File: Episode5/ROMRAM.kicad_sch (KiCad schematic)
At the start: 23 parts, among them SW1 Bank, SW2 RST SW, U10 AS6C1008, U11 HD63C09P, U12 MIC1232, U9 SST39SF010, X1 12MHz

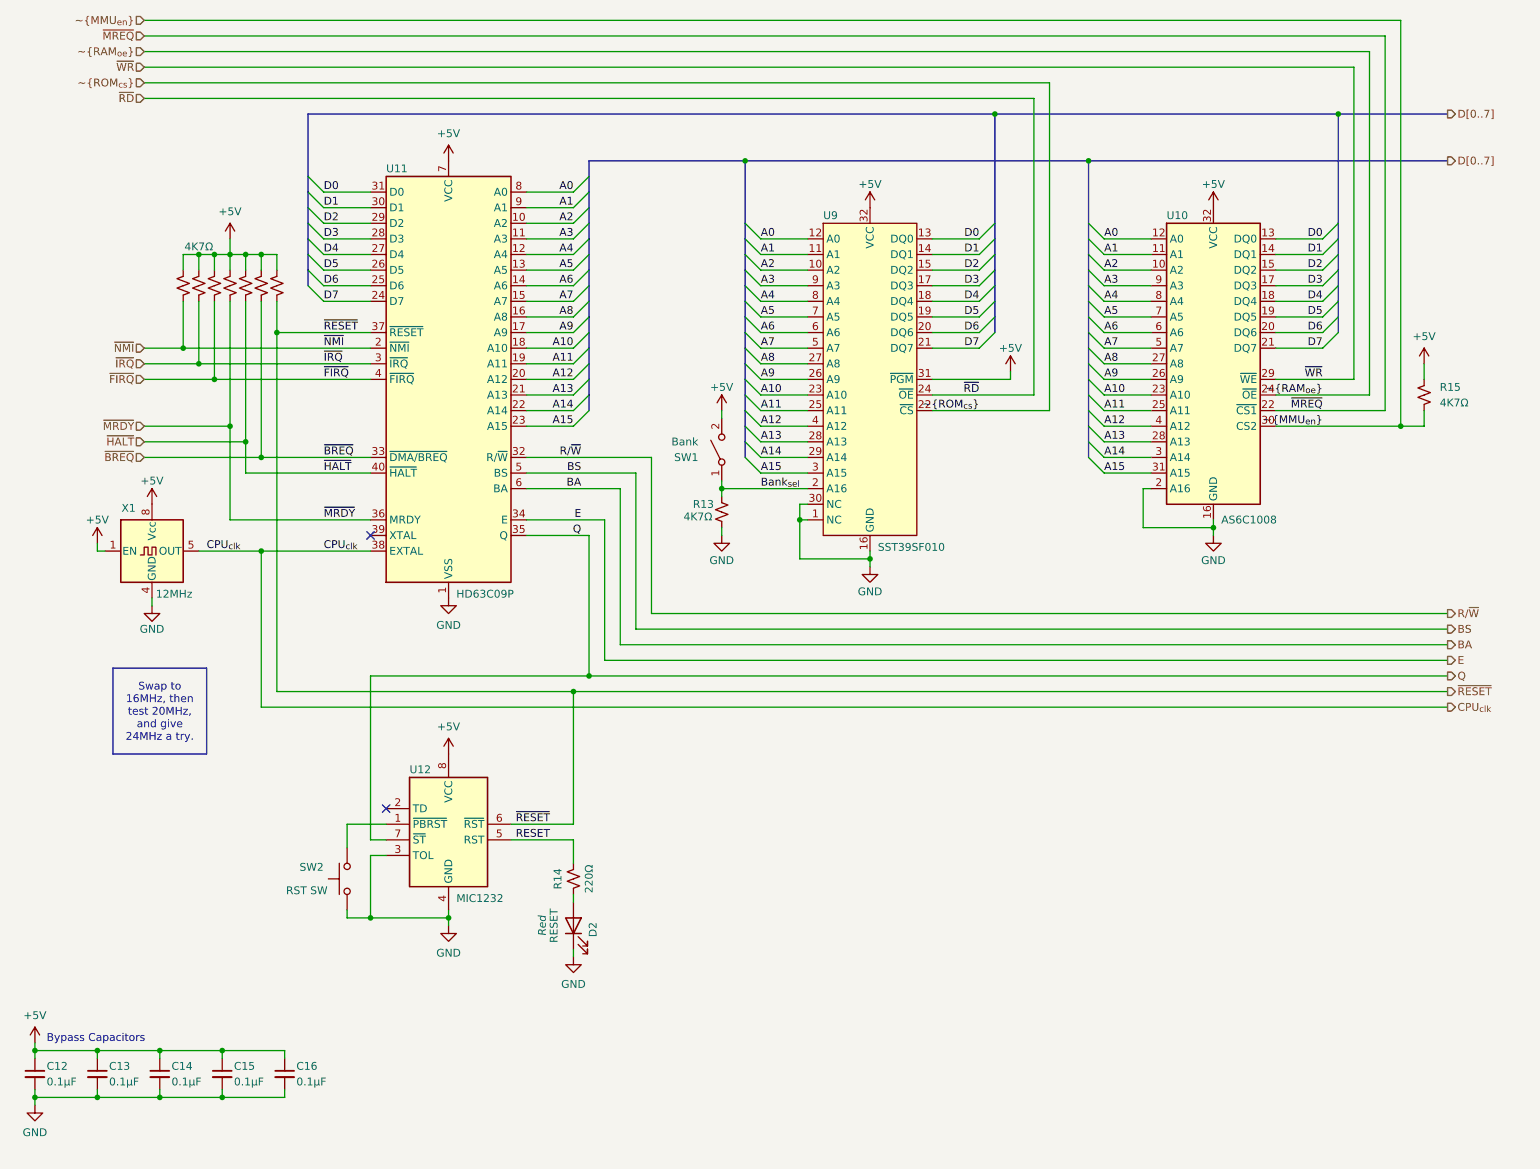
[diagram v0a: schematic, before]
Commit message: Placed Global labels instead. And toying with new PLDs
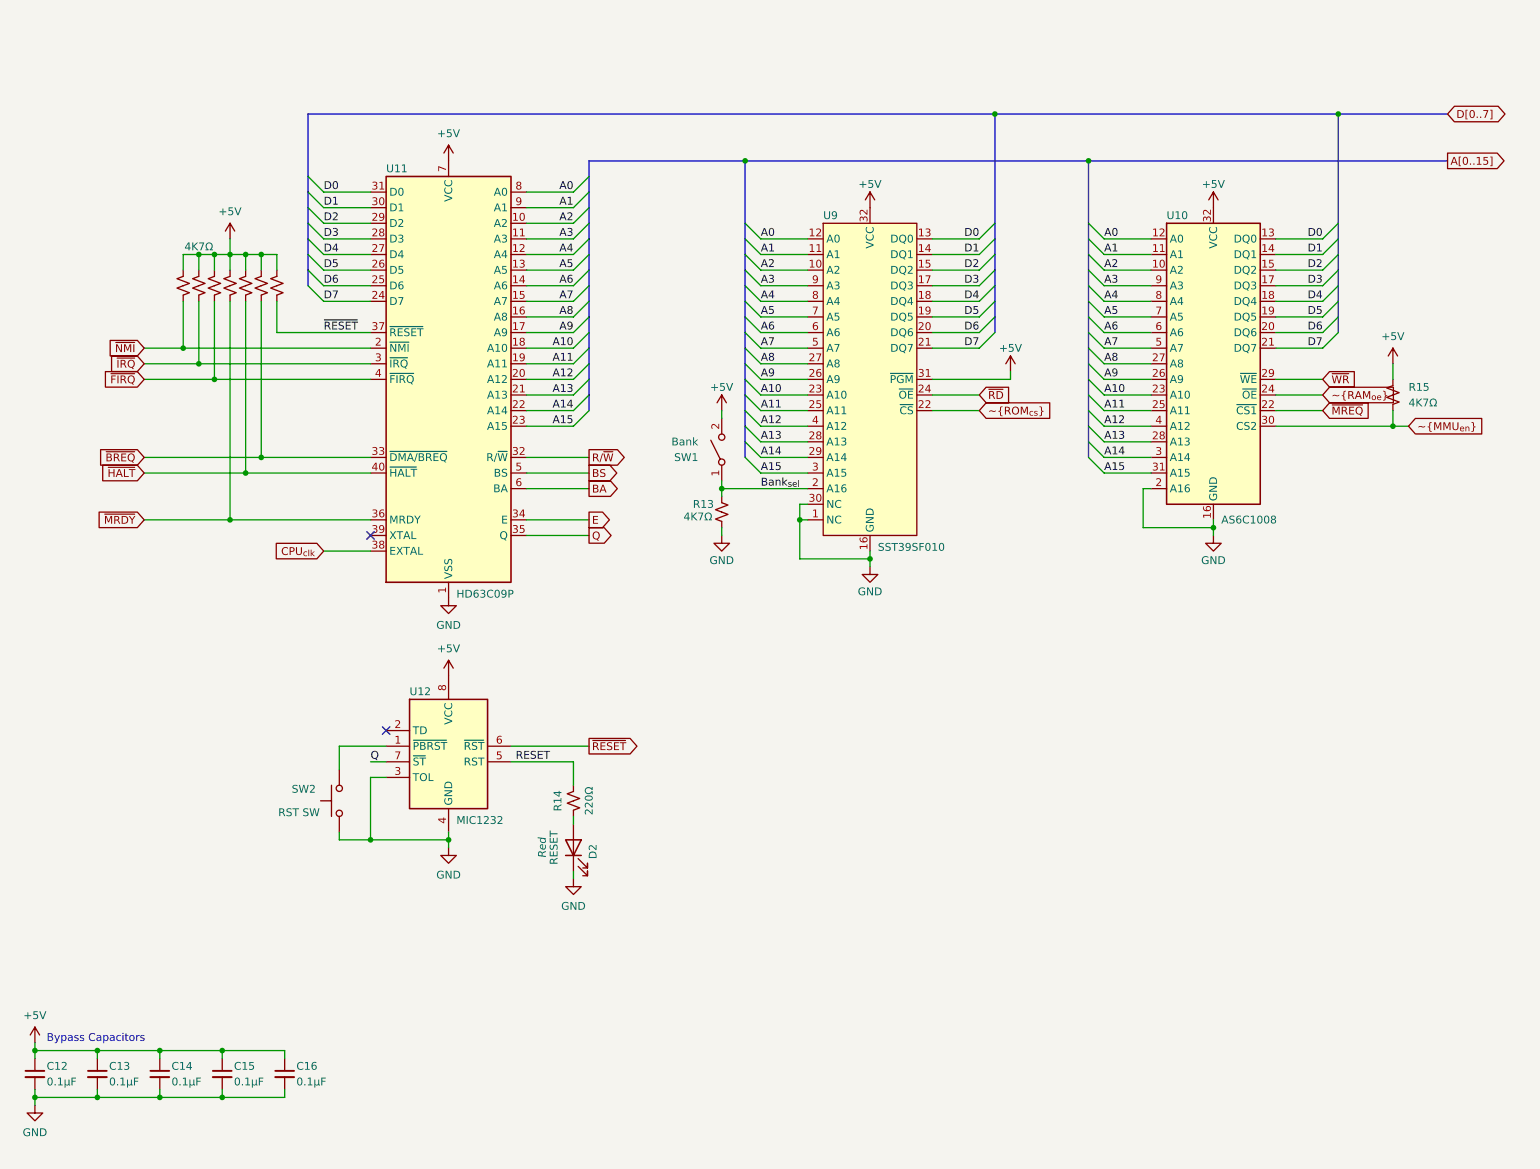
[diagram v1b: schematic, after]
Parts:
- removed X1: 12MHz, Oscillator:Oscillator_DIP-8, symbol Oscillator:CXO_DIP8
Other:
- moved on the sheet: D2, R14, R15, SW2, U12

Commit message: Toying with different alternatives for the CPU board
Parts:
- added X1: 16MHz, Oscillator:Oscillator_DIP-8, symbol Oscillator:CXO_DIP8
- renumbered C12 to C1, C13 to C2, C14 to C3, C15 to C4, C16 to C5, D2 to D1, R6 to R1, R14 to R10, R7 to R2, R8 to R3, R9 to R4, R10 to R5, R11 to R6, R12 to R7, R15 to R8, R13 to R9, U9 to U1, U10 to U2, U11 to U3, U12 to U4
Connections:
- net +5V: now also X1.1 (EN), X1.8 (Vcc)
- net CPU_{clk}: now also X1.5 (OUT)
- net GND: now also X1.4 (GND)
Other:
- moved on the sheet: D1, R10, SW2, U4

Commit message: Finished the preliminary design of the CPU card
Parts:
- removed C4, C5: 0.1µF, symbol Device:C_Small
- removed D1: RESET, symbol Device:LED
- removed R1, R2, R3, R4, R5, R6, R7: 4K7Ω, symbol Device:R_Small_US
- removed R10: 220Ω, symbol Device:R_Small_US
- removed SW2: RST SW, symbol Switch:SW_Push
- removed U3: HD63C09P, Package_DIP:DIP-40_W15.24mm_Socket, symbol CPU_NXP_6800:MC6809
- removed U4: MIC1232, Package_DIP:DIP-8_W7.62mm_Socket, symbol MicroHobbyist:MIC1232
- removed X1: 16MHz, Oscillator:Oscillator_DIP-8, symbol Oscillator:CXO_DIP8
- added JP1: CLR NVRAM, Connector_PinHeader_2.54mm:PinHeader_1x02_P2.54mm_Vertical, symbol Jumper:Jumper_2_Small_Open
- added U14: DS12C887A, Package_DIP:DIP-24_W15.24mm_Socket_LongPads, symbol 6309 Unleashed 2.0:DS12C887A
- SW3: renamed from SW1; value Bank -> BANK
- renumbered C1 to C18, C2 to C19, C3 to C20, R8 to R19, R9 to R20, U1 to U13, U2 to U15
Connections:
- net +5V: now also U14.1 (MOT), U14.24 (VCC)
- net D0: now also U14.4 (AD0)
- net D1: now also U14.5 (AD1)
- net D2: now also U14.6 (AD2)
- net D3: now also U14.7 (AD3)
- net D4: now also U14.8 (AD4)
- net D5: now also U14.9 (AD5)
- net D6: now also U14.10 (AD6)
- net D7: now also U14.11 (AD7)
- net GND: now also JP1.1 (A), U14.12 (GND)
- net R/~{W}: now also U14.15 (R/~{W})
- net ~{RESET}: now also U14.18 (~{RESET})
- net Bank_{sel} renamed BANK_{sel}
- new net: JP1.2 (B), U14.21 (~{RCLR})
- new net RTC_{as}: U14.14 (AS)
- new net RTC_{ds}: U14.17 (DS)
- new net SQW: U14.23 (SQW)
- new net ~{IRQ}0: U14.19 (~{IRQ})
- new net ~{RTC_{cs}}: U14.13 (~{CS})
- no-connect marks 2 -> 0
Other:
- company: Frédéric "MicroHobbyist" Segard -> MicroHobbyist
- title: (none) -> Flash ROM, SRAM, and RTC
- moved on the sheet: C18, C19, C20, R19, R20, SW3, U13, U15
